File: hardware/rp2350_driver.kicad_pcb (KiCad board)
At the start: 6 copper layers, 76 x 46.4 mm, 291 parts, among them J1 XT30, J10 Power Output, J11 CAN2 PLUG, J12 Conn_01x06, J2 XT30, J3 USB_C_Receptacle_USB2.0, J4 SM03B-SRSS-TB, J5 Estop Conn, J6 SM03B-SRSS-TB, J7 Conn_01x03, J8 Conn_01x03, J9 XT30, Q1 Q_PNP_BEC, Q2 Q_PNP_BEC, Q3 Q_PNP_BEC, Q4 Q_PNP_BEC, Q5 Q_NMOS_GDS, SW1 Button, SW2 Button, U1 EG3113, U10 INA240A1D, U101 FUSB302BMPX, U11 USBLC6-2P6, U12 EG3113, U13 TS5A3159DCK, U14 TS5A3159DCK, U15 TS5A3159DCK, U16 CA-IS3052CG, U17 TS5A3159DCK, U18 SIT3088ETK, U19 SIT3088ETK, U20 SIT3088ETK, U21 SIT3088ETK, U22 TS5A3159DCK, U23 TS5A3159DCK, U24 TS5A3159DCK, U25 TS5A3159DCK, U26 TS5A3159DCK, U27 TS5A3159DCK, U28 XL7005A, U29 LM74700, U3 W25Q16JV, U4 SPX3819M5-L-3-3, U5 INA240A1D, U6 EG3113, U7 EG3113, U8 RP2350_80QFN, U9 INA240A1D, Y1 ABM8-272-T3

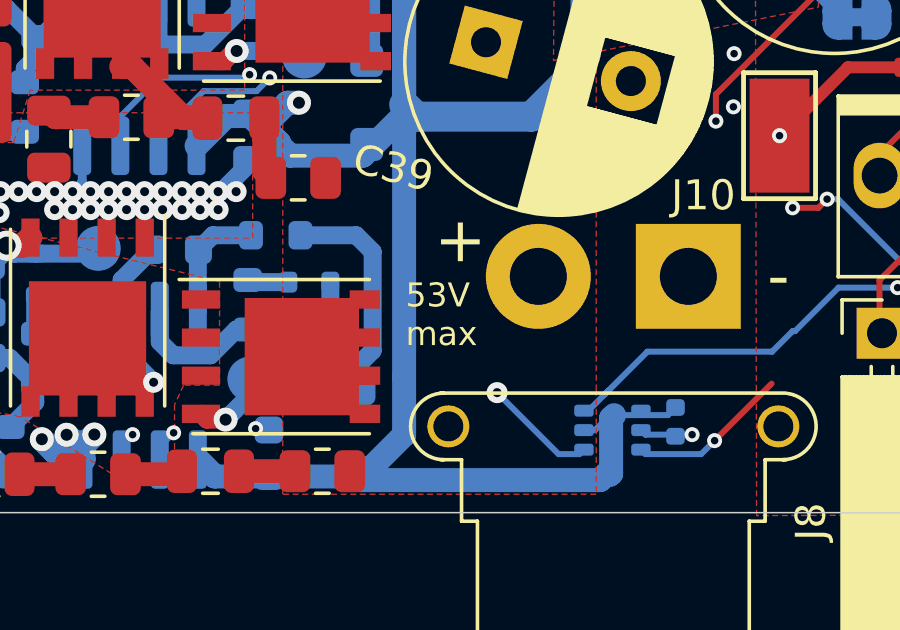
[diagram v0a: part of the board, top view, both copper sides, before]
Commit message: remove incorrect max voltage silk
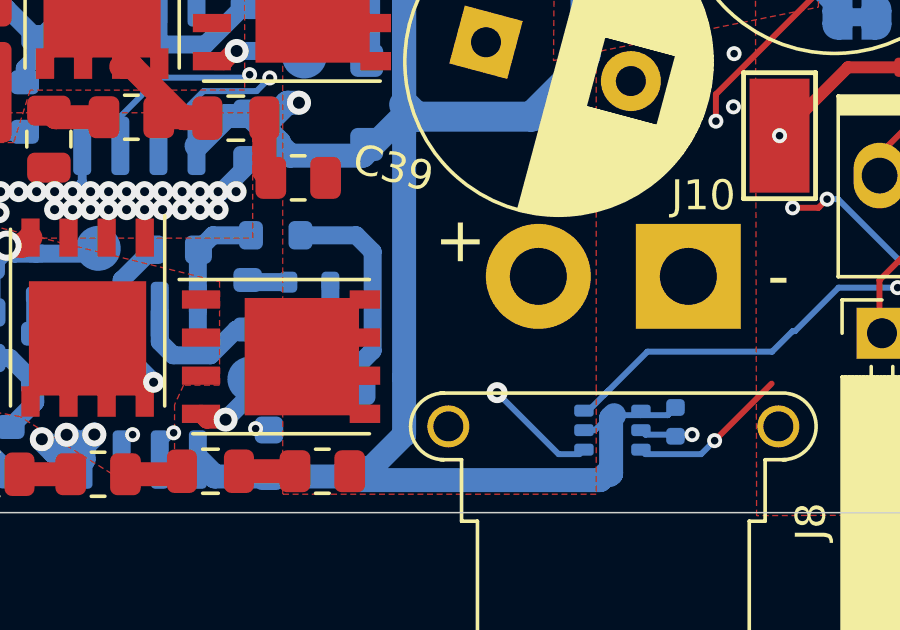
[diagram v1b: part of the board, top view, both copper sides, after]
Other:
- board text removed: "53V max"
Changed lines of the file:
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@@
-		)
-	)
-	(gr_text "53V\nmax"
-		(at 149.2 121.8 0)
-		(layer "F.SilkS")
-		(effects
-			(font
-				(size 0.8 0.8)
-				(thickness 0.2)
-			)
-			(justify left)
 		)
 	)
